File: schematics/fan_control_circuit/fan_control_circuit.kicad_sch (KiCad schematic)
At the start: 13 parts

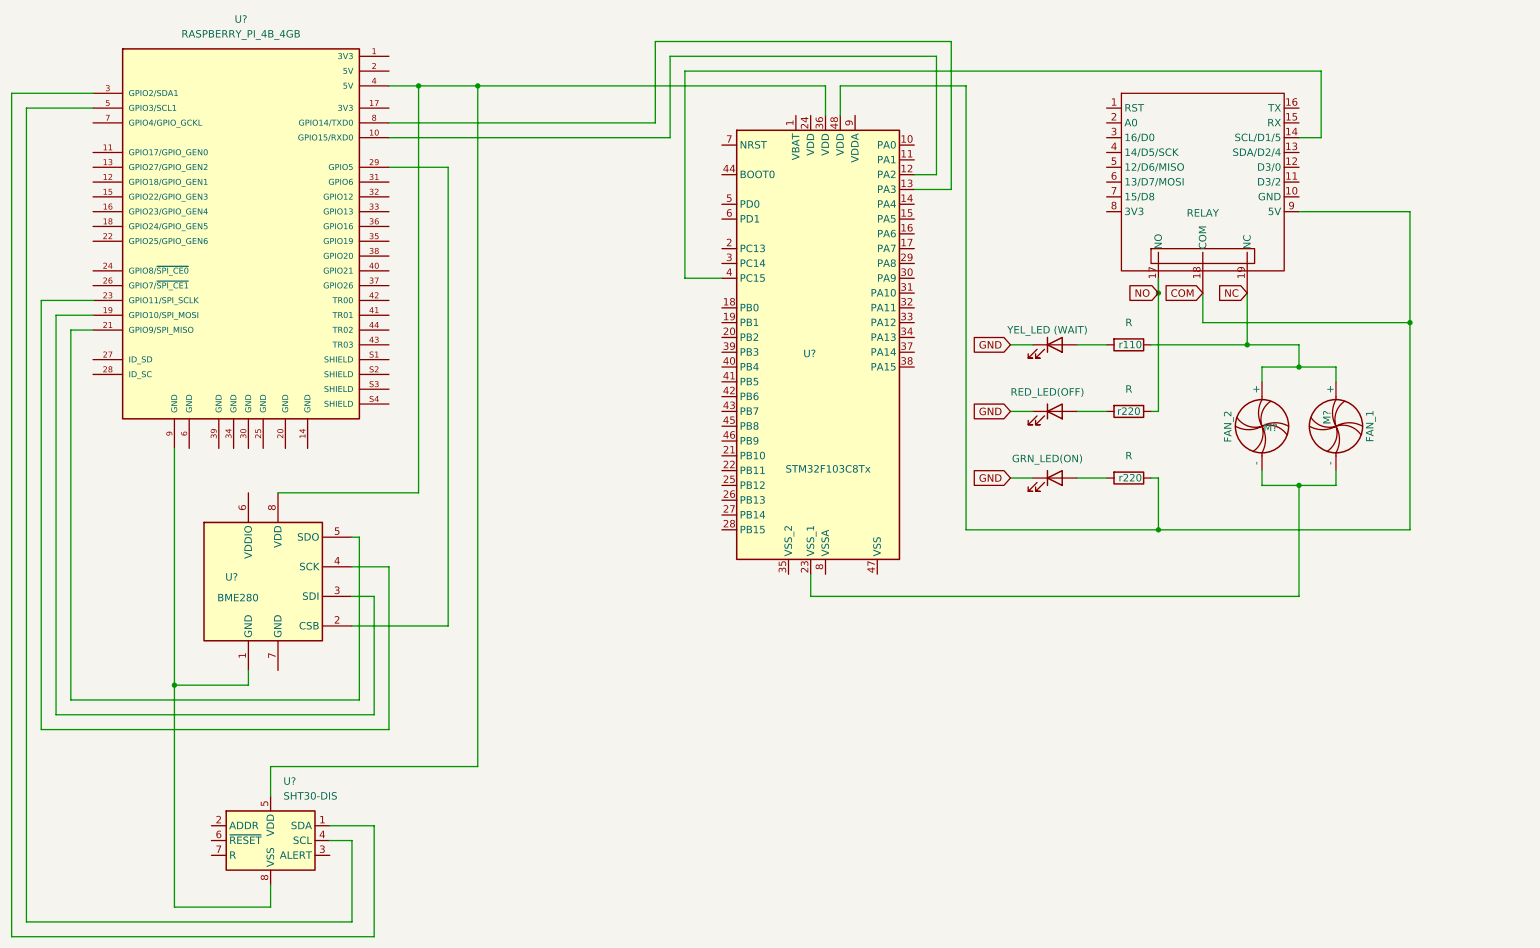
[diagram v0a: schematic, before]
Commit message: updates to schematic for tmp36 sensor
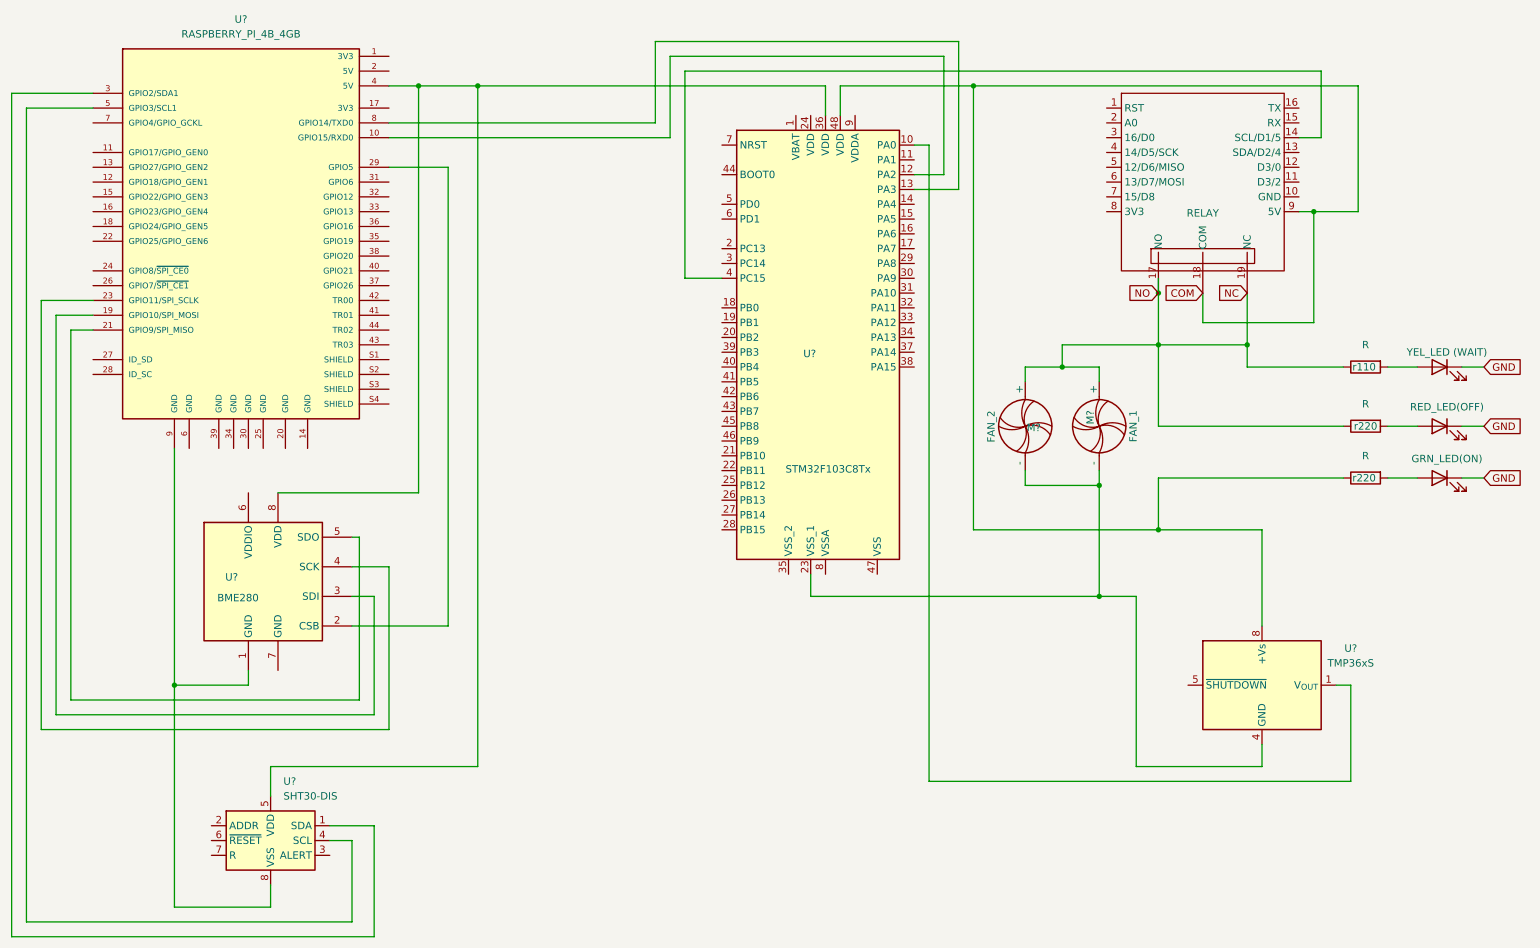
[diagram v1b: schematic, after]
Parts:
- added U?: TMP36xS, Package_SO:SOIC-8_3.9x4.9mm_P1.27mm, symbol Sensor_Temperature:TMP36xS
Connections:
- net NO is gone; now on net NC: RELAY.17 (NO), r220.1
- net COM: now also U?.8 (+Vs)
- net at M?.2 (-), M?.2 (-), U?.23 (VSS_1): now also U?.4 (GND)
- net at U?.10 (PA0): now also U?.1 (V_{OUT})
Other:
- moved on the sheet: M?, r110, r220

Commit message: updating schematic
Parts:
- added C470: C_Polarized, symbol Device:C_Polarized_US
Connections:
- net COM: now also C470.1
- net NC: no longer RELAY.17 (NO), r220.1
- net at RELAY.10 (GND): now also C470.2
- net at RELAY.15 (RX): now also U?.12 (PA2)
- net at RELAY.16 (TX): now also U?.13 (PA3)
- net at U?.4 (5V), U?.5 (VDD), U?.8 (VDD): now also U?.24 (VDD); no longer U?.36 (VDD)
- net at U?.10 (GPIO15/RXD0): now also U?.21 (PB10); no longer U?.12 (PA2)
- net at U?.8 (GPIO14/TXD0): now also U?.22 (PB11); no longer U?.13 (PA3)
- new net NO: RELAY.17 (NO), r220.1
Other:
- moved on the sheet: U?

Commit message: updates to schematic. thinking about hardware situation
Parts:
- removed C470: C_Polarized, symbol Device:C_Polarized_US
- added C1: 470uF, Capacitor_SMD:CP_Elec_3x5.3, symbol Device:C_Polarized_Small_US
- added D?: BLU (ON), LED_SMD:LED-APA102-2020, symbol Device:LED
- D1: renamed from D?; value YEL_LED (WAIT) -> YEL(WAIT); footprint (none) -> LED_SMD:LED-APA102-2020
- D2: renamed from D?; value RED_LED(OFF) -> RED(OFF); footprint (none) -> LED_SMD:LED-APA102-2020
- D3: renamed from D?; value GRN_LED(ON) -> GRN(ON); footprint (none) -> LED_SMD:LED-APA102-2020
- F1: renamed from M?; value FAN_2 -> Fan2; footprint (none) -> Connector_PinHeader_2.54mm:PinHeader_1x01_P2.54mm_Horizontal
- F2: renamed from M?; value FAN_1 -> Fan1; footprint (none) -> Connector_PinHeader_2.54mm:PinHeader_1x01_P2.54mm_Horizontal
- R1: renamed from r110; value R -> 110; footprint (none) -> OptoDevice:R_LDR_4.9x4.2mm_P2.54mm_Vertical
- R2, R3: renamed from r220; value R -> 220; footprint (none) -> OptoDevice:R_LDR_4.9x4.2mm_P2.54mm_Vertical
- gave numbers to parts that had none: 5
- renumbered RELAY to RELAY1
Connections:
- net COM: now also C1.1
- net GND: now also D?.1 (K)
- net at RELAY1.10 (GND): now also C1.2
- net at RELAY1.15 (RX): no longer U4.12 (PA2)
- net at RELAY1.16 (TX): no longer U4.13 (PA3)
- net at U4.2 (PC13): now also D?.2 (A)
- net at U4.21 (PB10): no longer U1.10 (GPIO15/RXD0)
- net at U4.22 (PB11): no longer U1.8 (GPIO14/TXD0)
- net at U4.42 (PB6): now also U1.10 (GPIO15/RXD0)
- net at U4.43 (PB7): now also U1.8 (GPIO14/TXD0)
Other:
- moved on the sheet: U3
